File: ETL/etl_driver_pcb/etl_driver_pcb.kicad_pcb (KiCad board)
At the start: 2 copper layers, 69.6 x 33.5 mm, 15 parts, among them J1 Analog in, J2 12V power, J3 to_ETL, Q1 BD441, U1 CA3140

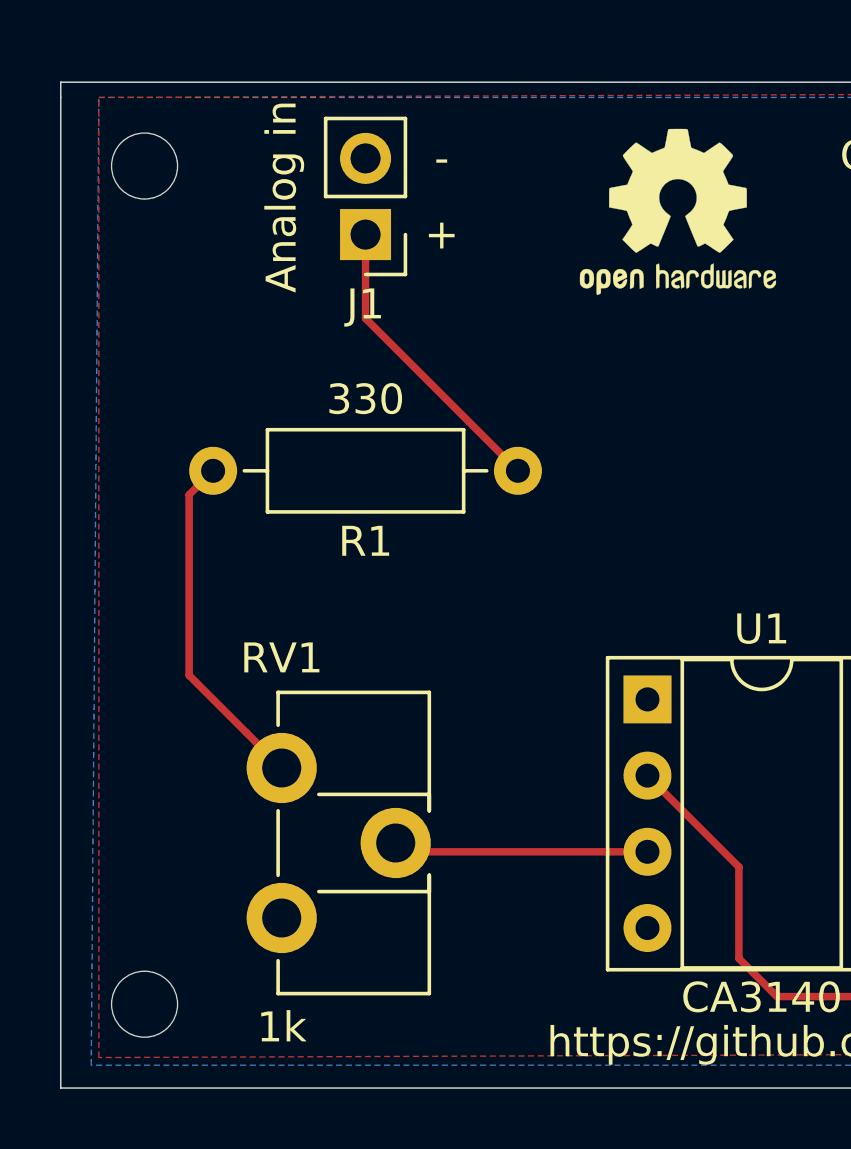
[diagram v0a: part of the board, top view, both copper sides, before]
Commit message: add arduino due shield for lens driver
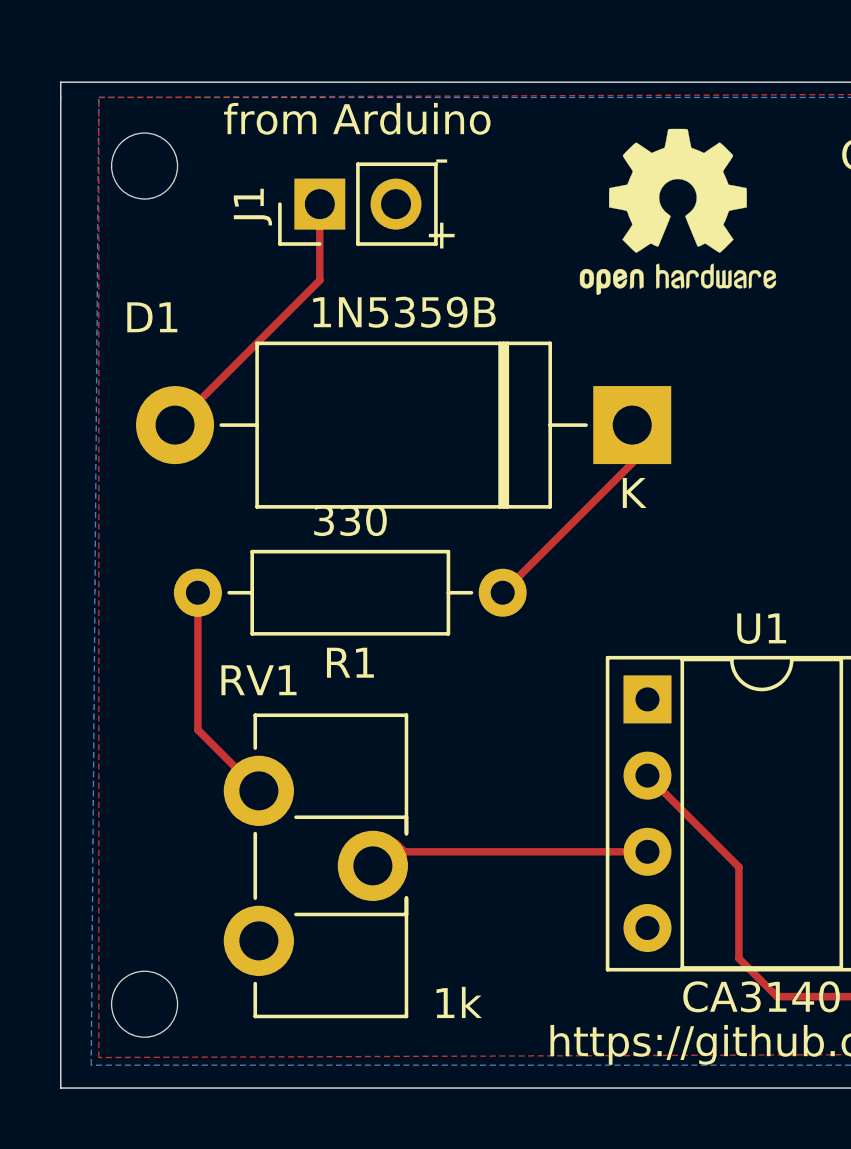
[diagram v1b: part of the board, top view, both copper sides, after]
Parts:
- added D1: 1N5359B, Diode_THT:D_DO-201_P15.24mm_Horizontal, F.Cu at (143.0, 108.0)
- J1: value Analog in -> from Arduino
- moved R1 4.10 mm to (138.7, 113.5)
- moved J1 1.83 mm to (132.6, 100.6), turned to 90 degrees
- moved RV1 1.08 mm to (130.6, 120.1)
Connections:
- J1 pad 1: Net-(J1-Pad1) -> Net-(D1-Pad2)
- R1 pad 1: Net-(J1-Pad1) -> Net-(D1-Pad1)
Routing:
- net Net-(J1-Pad1): track 9.98 -> 0.00 mm
- net Net-(D1-Pad2): track 0.00 -> 9.36 mm
- net Net-(D1-Pad1): track 0.00 -> 7.38 mm
- net Net-(R1-Pad2): track 11.5 -> 7.45 mm
